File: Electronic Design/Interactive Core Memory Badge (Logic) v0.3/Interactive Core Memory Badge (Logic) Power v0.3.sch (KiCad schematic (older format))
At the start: 18 parts, among them J3 Conn_01x03_Male, J4 Conn_01x02_Male, J5 Conn_01x02_Male, Q1 IRLML6344TRPBF, SW1 SW_DPDT_x2, U1 LD1117S33TR_SOT223

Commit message: Schematic refinement
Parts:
- removed J3: Conn_01x03_Male, symbol Connector:Conn_01x03_Male
- removed J5: Conn_01x02_Male, symbol Connector:Conn_01x02_Male
- added J3: BM03B-PASS-1-TFT__LF__SN_, JST_BM03B-PASS-1-TFT:BM03BPASS1TFTLFSN, symbol BM03B-PASS-1-TFT__LF__SN_:BM03B-PASS-1-TFT__LF__SN_
- added R51, R52: 10k, Resistor_SMD:R_0805_2012Metric, symbol Device:R
- D1: footprint Digikey:DO-214AC -> Diode_SMD:D_SMA_Handsoldering
- J4: footprint (none) -> Connector_PinSocket_2.54mm:PinSocket_1x02_P2.54mm_Vertical_SMD_Pin1Left
- R43: value 0.01 -> 0.001
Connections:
- net labels added: VSW_HALF_VOL_MONITOR
- net labels removed: FEATHER_GND, FEATHER_VBAT, FEATHER_VBUS
- wire segments 51 -> 47
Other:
- note added: "ALL SYSTEM\nSTAR GROUNDING"
- note added: "ALTERNATE CONNECTOR - Generic SMT 2-pin .1” \nheader option for everything else."
- note added: "BOTH MODES REQUIRE:\nVIN must be supplied TO the Teensy\n(because VIN-VUSB is cut) and the \nCore 64 Logic Board provides it here."
- note added: "DIGITAL\nLOGIC GROUND"
- note added: "Diode provides 1.1V drop if using USB power.\n Keeps +VSW close to 4V to reduce 3.3V regulator strain.\n Prevents current flow back to USB and provides \n additional reverse polarity protection."
- note added: "HACKER UPGRADE TO USE FEATHER-TEENSY ADAPTER BOARD REQUIRES:\nA) REPLACE THE ALKALINE/NIMH BATTERY PACK WITH 1S LIPO IN THE SAME POWER PORT, OR THE ALTERNATE PORT.\n -or-\nB) REMOVE THE ALKALINE/NIMH BATTERY PACK AND CONNECT 1S LIPO DIRECTLY TO FEATHER JST-PH BATTERY/CHARGING PORT."
- note added: "HIGH POWER\nSYSTEM GROUND"
- note added: "MODE 2\n USB 5V through Teensy LC or 3.2 \n VUSB is 5V from USB cable."
- note added: "POWER SWITCH AND VOLTAGE MONITOR"
- note added: "REVERSE POLARITY\nPROTECTION"
- note added: "SYSTEM CURRENT\nMEASUREMENT"
- note added: "TEENSY LC OR 3.2 AND ALKALINE/NIMH BATTERY PACK\n*** MUST CUT VIN-VUSB TRACE ON TEENSY ***\nTHIS IS THE STANDARD MANUFACTURED KIT CONFIGURATION"
- note removed: "BOTH MODES REQUIRE:\nVIN must be supplied TO the Teensy and\nthe Core 64 Logic Board provides it here."
- note removed: "DIGITAL LOGIC GROUND"
- note removed: "Diode provides 1.1V drop if using USB power.\n Keeps +VSW close to 4V to reduce 3.3V regulator strain.\n Prevents current flow back to USB and provides additional reverse polarity protection."
- note removed: "HACKER UPGRADE TO USE FEATHER REQUIRES EITHER:\nA) REPLACE THE ALKALINE/NIMH BATTERY PACK WITH 1S LIPO IN THE SAME POWER PORT, OR ONE OF THE ALTERNATE PORTS\n>>> ALTERNATE CONNECTOR 1 - Adafruit (1769) SMT 2-pin JST-PH (used with the Feather and Adafruit batteries)\n>>> ALTERNATE CONNECTOR 2 - Generic SMT 2-pin .1” header option for everything else. \nB) REMOVE THE ALKALINE/NIMH BATTERY PACK AND 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"
- note removed: "MODE 2\n USB 5V through Teensy LC or 3.2 \n VUSB is 5V from USB cable.\n VIN must be supplied TO the Teensy and Core 64 Logic Board provides it."
- note removed: "MODE 3\n USER REPLACED 1S LIPO BATTERY 3.7 OR 4.2V\n THE FEATHER WILL TRY TO CHARGE THE BATTERY AT 100MA WHEN USB POWER IS CONNECTED. \n FAILURE TO USE A 1S LIPO WILL DESTROY THE CHARGER CIRCUIT ON THE FEATHER."
- note removed: "MODE 4\n USB 5V through the Feather.\n Automatically recharges a connected 1s LiPo at 100mA."
- note removed: "POWER SWITCH"
- note removed: "REVERSE POLARITY PROTECTION"
- note removed: "STAR GROUND AS MUCH AS POSSIBLE REVERSE\nPOLARITY FET TO GNDD (DIGITAL) AND GND (POWER)."
- note removed: "SYSTEM CURRENT MEASUREMENT"
- note removed: "TEENSY LC OR 3.2 AND ALKALINE/NIMH BATTERY PACK\n*** MUST CUT VIN-VUSB TRACE ***\nTHIS IS THE STANDARD MANUFACTURED KIT CONFIGURATION"
- note removed: "TO DO: Connect to analog inputs of MCU for self-test and diagnostics."
- note removed: "TO DO: Does Feather receive power to MCU directly from battery?\nDoes Feather require a battery to be connected in order to work?"
- note removed: "TO DO: Teensy and feather power to -Batt or GND? \nDo they need to avoid the reverse polarity detector? \nOr will they interfere?"
- note removed: "TWO ALTERNATIVE POWER MODES SELECTED BY DOUBLE-THROW SWITCH:"
- moved on the sheet: C3, D1, F1, J4, Q1, R1, SW1A, TP1, TP2, TP3, TP4, TP5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

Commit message: Added OLED power solder jumpers
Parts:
- Q1: footprint Package_TO_SOT_SMD:SOT-23 -> Digikey:SOT-23-3
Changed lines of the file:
@@
 F 0 "Q1" V 1701 6650 50  0000 C CNN
 F 1 "IRLML6344TRPBF" V 1794 6650 50  0000 C CNN
-F 2 "Package_TO_SOT_SMD:SOT-23" H 1650 6575 50  0001 L CIN
+F 2 "Digikey:SOT-23-3" H 1650 6575 50  0001 L CIN
 F 3 "https://www.digikey.com/product-detail/en/infineon-technologies/IRLML6344TRPBF/IRLML6344TRPBFCT-ND/2538168" H 1450 6650 50  0001 L CNN
 	1    1450 6650

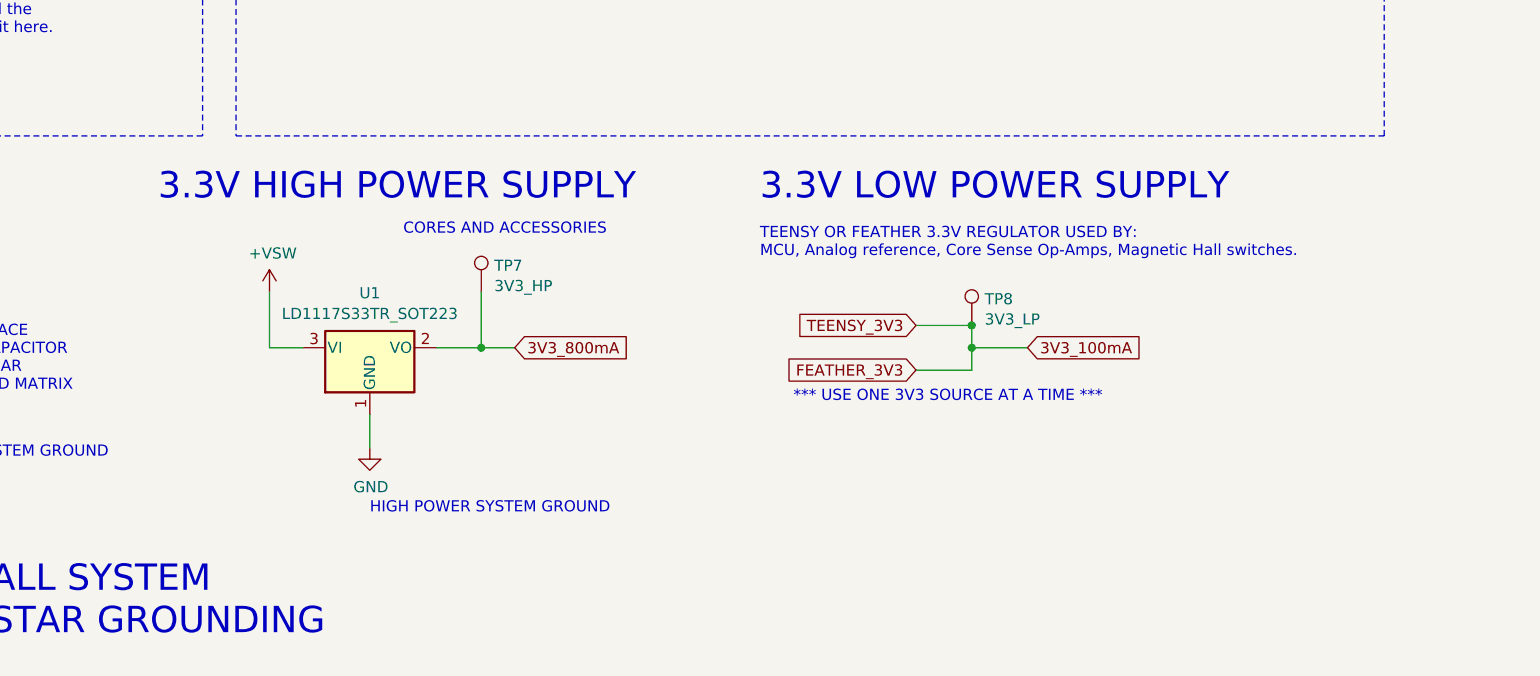
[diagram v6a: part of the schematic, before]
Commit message: Overall PCB layout placements
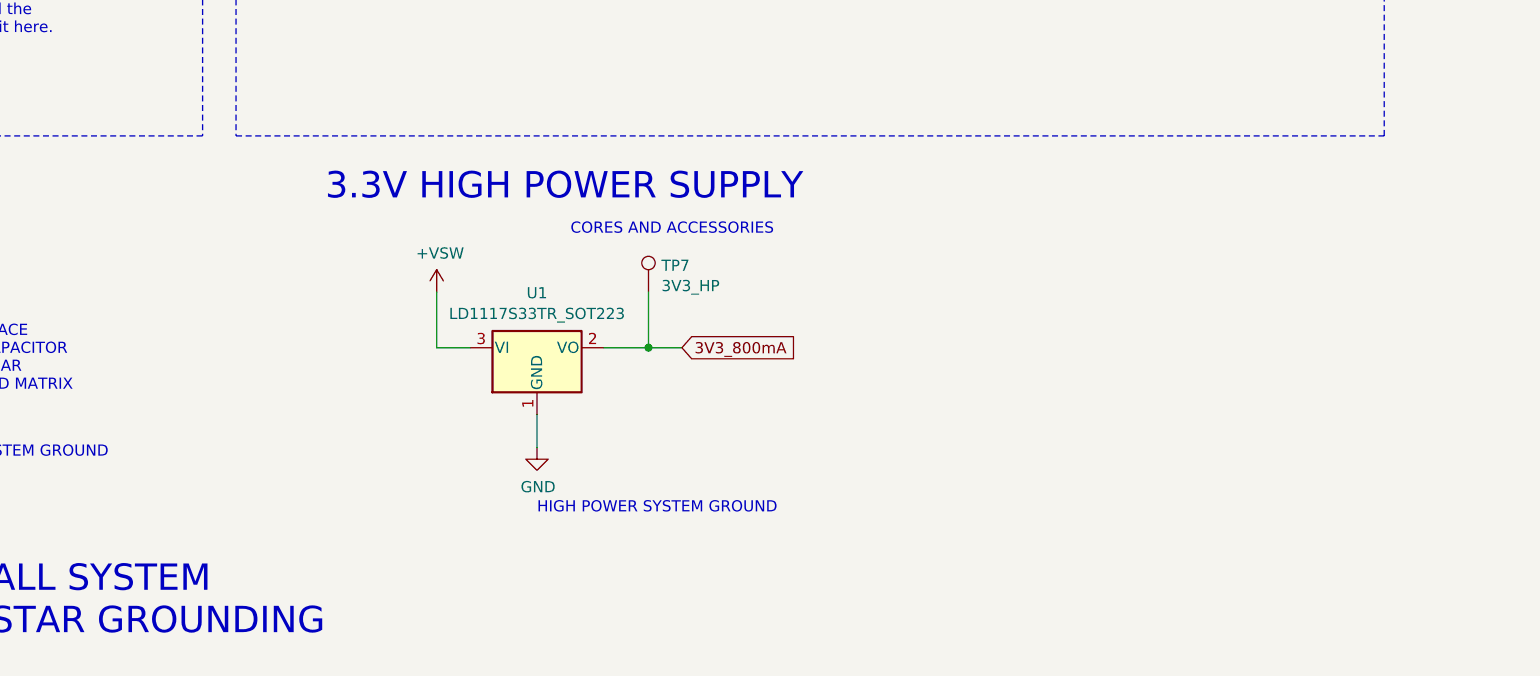
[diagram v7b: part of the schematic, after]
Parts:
- removed TP8: 3V3_LP, TestPoint:TestPoint_Keystone_5000-5004_Miniature, symbol Connector:TestPoint
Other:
- note removed: "*** USE ONE 3V3 SOURCE AT A TIME ***"
- note removed: "3.3V LOW POWER SUPPLY"
- note removed: "TEENSY OR FEATHER 3.3V REGULATOR USED BY:\nMCU, Analog reference, Core Sense Op-Amps, Magnetic Hall switches."
- moved on the sheet: TP7, U1
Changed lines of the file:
@@
 $EndComp
 Wire Wire Line
-	6950 4900 7150 4900
+	7700 4900 7900 4900
 Text GLabel 1000 4900 0    50   Input ~ 0
 5V_USB
@@
 	-1   0    0    1
 $EndComp
-Text Notes 6800 4400 0    50   ~ 0
+Text Notes 7550 4400 0    50   ~ 0
 CORES AND ACCESSORIES
 $Comp
@@
 $EndComp
 Wire Wire Line
-	7150 4900 7300 4900
-Connection ~ 7150 4900
-Wire Wire Line
-	7150 4650 7150 4900
+	7900 4900 8050 4900
+Connection ~ 7900 4900
+Wire Wire Line
+	7900 4650 7900 4900
 $Comp
 L Switch:SW_DPDT_x2 SW1
@@
 L Regulator_Linear:LD1117S33TR_SOT223 U1
 U 1 1 5E7B5B14
-P 6650 4900
+P 7400 4900
 AR Path="/5E7548ED/5E7B5B14" Ref="U1"  Part="1"
 AR Path="/5E755AC8/5D254AE8/5E7B5B14" Ref="U?"  Part="1"
-F 0 "U1" H 6650 5145 50  0000 C CNN
-F 1 "LD1117S33TR_SOT223" H 6650 5052 50  0000 C CNN
-F 2 "Package_TO_SOT_SMD:SOT-223-3_TabPin2" H 6650 5100 50  0001 C CNN
-F 3 "http://www.st.com/st-web-ui/static/active/en/resource/technical/document/datasheet/CD00000544.pdf" H 6750 4650 50  0001 C CNN
-	1    6650 4900
+F 0 "U1" H 7400 5145 50  0000 C CNN
+F 1 "LD1117S33TR_SOT223" H 7400 5052 50  0000 C CNN
+F 2 "Package_TO_SOT_SMD:SOT-223-3_TabPin2" H 7400 5100 50  0001 C CNN
+F 3 "http://www.st.com/st-web-ui/static/active/en/resource/technical/document/datasheet/CD00000544.pdf" H 7500 4650 50  0001 C CNN
+	1    7400 4900
 	1    0    0    -1
 $EndComp
@@
 REVERSE POLARITY\nPROTECTION
 Wire Wire Line
-	6200 4900 6350 4900
+	6950 4900 7100 4900
 Text Notes 750  2200 0    50   ~ 0
 MODE 1\n  BUILT-IN BATTERY PACK (Keystone 2482CN) WITH 4X “AAA” ALKALINE OR NIMH CELLS\n  …or 3-4 “AA” alkaline/NiMh, or 1S LiPo, but the logic board does not recharge these batteries automatically from USB power.\n  CONNECTED TO 3 PIN input for Battery Pack\n  On PCB: SMT CONN, 3 TERM, HORZ, 2mm spacing, detent lock\n  Such as: Keystone 976, JST PA BM03B-PASS-1-TFT(LF)(SN), Adafruit 4391 (JST PH 3-pin aka STEMMA)\n  from KAWEEI Technology CW2001-03T-H01-BD-A,
@@
 Text GLabel 4450 3800 0    50   Input ~ 0
 TEENSY_VIN
-Text GLabel 9100 4800 0    50   Input ~ 0
-TEENSY_3V3
 Text GLabel 1600 3550 0    50   Input ~ 0
 TEENSY_GND
@@
 Text Notes 3950 3500 0    50   ~ 0
 BOTH MODES REQUIRE:\nVIN must be supplied TO the Teensy\n(because VIN-VUSB is cut) and the \nCore 64 Logic Board provides it here.
-Text Notes 8400 4500 0    50   ~ 0
-TEENSY OR FEATHER 3.3V REGULATOR USED BY:\nMCU, Analog reference, Core Sense Op-Amps, Magnetic Hall switches.
-Text GLabel 9100 5000 0    50   Input ~ 0
-FEATHER_3V3
-Text GLabel 9600 4900 2    50   Input ~ 0
-3V3_100mA
-Wire Wire Line
-	9100 4800 9350 4800
-Wire Wire Line
-	9350 4800 9350 4900
-Wire Wire Line
-	9350 4900 9600 4900
-Wire Wire Line
-	9350 4900 9350 5000
-Wire Wire Line
-	9350 5000 9100 5000
-Connection ~ 9350 4900
 $Comp
 L power:+VSW #PWR0113
 U 1 1 5E8659D4
-P 6200 4650
+P 6950 4650
 AR Path="/5E7548ED/5E8659D4" Ref="#PWR0113"  Part="1"
 AR Path="/5E755AC8/5D254AE8/5E8659D4" Ref="#PWR?"  Part="1"
-F 0 "#PWR0113" H 6200 4500 50  0001 C CNN
-F 1 "+VSW" H 6215 4823 50  0000 C CNN
-F 2 "" H 6200 4650 50  0001 C CNN
-F 3 "" H 6200 4650 50  0001 C CNN
-	1    6200 4650
-	1    0    0    -1
-$EndComp
-Wire Wire Line
-	6200 4650 6200 4900
-Text GLabel 7300 4900 2    50   Input ~ 0
+F 0 "#PWR0113" H 6950 4500 50  0001 C CNN
+F 1 "+VSW" H 6965 4823 50  0000 C CNN
+F 2 "" H 6950 4650 50  0001 C CNN
+F 3 "" H 6950 4650 50  0001 C CNN
+	1    6950 4650
+	1    0    0    -1
+$EndComp
+Wire Wire Line
+	6950 4650 6950 4900
+Text GLabel 8050 4900 2    50   Input ~ 0
 3V3_800mA
 Wire Wire Line
@@
 Text Notes 550  4250 0    118  ~ 0
 POWER SWITCH AND VOLTAGE MONITOR
-Text Notes 8400 4250 0    118  ~ 0
-3.3V LOW POWER SUPPLY
-Text Notes 5700 4250 0    118  ~ 0
+Text Notes 6450 4250 0    118  ~ 0
 3.3V HIGH POWER SUPPLY
-$Comp
-L Connector:TestPoint TP8
-U 1 1 5E88D7B5
-P 9350 4800
-AR Path="/5E7548ED/5E88D7B5" Ref="TP8"  Part="1"
-AR Path="/5E755AC8/5D254AE8/5E88D7B5" Ref="TP?"  Part="1"
-F 0 "TP8" H 9408 4918 50  0000 L CNN
-F 1 "3V3_LP" H 9408 4827 50  0000 L CNN
-F 2 "TestPoint:TestPoint_Keystone_5000-5004_Miniature" H 9550 4800 50  0001 C CNN
-F 3 "~" H 9550 4800 50  0001 C CNN
-	1    9350 4800
-	1    0    0    -1
-$EndComp
 $Comp
 L Connector:TestPoint TP7
 U 1 1 5E88DBA6
-P 7150 4650
+P 7900 4650
 AR Path="/5E7548ED/5E88DBA6" Ref="TP7"  Part="1"
 AR Path="/5E755AC8/5D254AE8/5E88DBA6" Ref="TP?"  Part="1"
-F 0 "TP7" H 7208 4768 50  0000 L CNN
-F 1 "3V3_HP" H 7208 4677 50  0000 L CNN
-F 2 "TestPoint:TestPoint_Keystone_5000-5004_Miniature" H 7350 4650 50  0001 C CNN
-F 3 "~" H 7350 4650 50  0001 C CNN
-	1    7150 4650
+F 0 "TP7" H 7958 4768 50  0000 L CNN
+F 1 "3V3_HP" H 7958 4677 50  0000 L CNN
+F 2 "TestPoint:TestPoint_Keystone_5000-5004_Miniature" H 8100 4650 50  0001 C CNN
+F 3 "~" H 8100 4650 50  0001 C CNN
+	1    7900 4650
 	1    0    0    -1
 $EndComp
@@
 L power:GND #PWR0116
 U 1 1 5E8C4F56
-P 6650 5350
+P 7400 5350
 AR Path="/5E7548ED/5E8C4F56" Ref="#PWR0116"  Part="1"
 AR Path="/5E755AC8/5D254AE8/5E8C4F56" Ref="#PWR?"  Part="1"
-F 0 "#PWR0116" H 6650 5100 50  0001 C CNN
-F 1 "GND" H 6655 5175 50  0000 C CNN
-F 2 "" H 6650 5350 50  0001 C CNN
-F 3 "" H 6650 5350 50  0001 C CNN
-	1    6650 5350
-	1    0    0    -1
-$EndComp
-Wire Wire Line
-	6650 5200 6650 5350
+F 0 "#PWR0116" H 7400 5100 50  0001 C CNN
+F 1 "GND" H 7405 5175 50  0000 C CNN
+F 2 "" H 7400 5350 50  0001 C CNN
+F 3 "" H 7400 5350 50  0001 C CNN
+	1    7400 5350
+	1    0    0    -1
+$EndComp
+Wire Wire Line
+	7400 5200 7400 5350
 Text Notes 2650 6200 0    118  ~ 0
 SYSTEM CURRENT\nMEASUREMENT
@@
 	1    0    0    -1
 $EndComp
-Connection ~ 9350 4800
 $Comp
 L Device:CP1_Small C?
@@
 	1    0    0    -1
 $EndComp
-Text Notes 6650 5650 0    50   ~ 0
+Text Notes 7400 5650 0    50   ~ 0
 HIGH POWER SYSTEM GROUND
 Text Notes 4400 5400 0    50   ~ 0
@@
 Text Notes 2050 3850 0    50   ~ 0
 HIGH POWER SYSTEM GROUND
-Text Notes 8550 5150 0    50   ~ 0
-*** USE ONE 3V3 SOURCE AT A TIME ***
 Text Notes 4000 4650 0    50   ~ 0
 LED ARRAY, TEENSY VIN

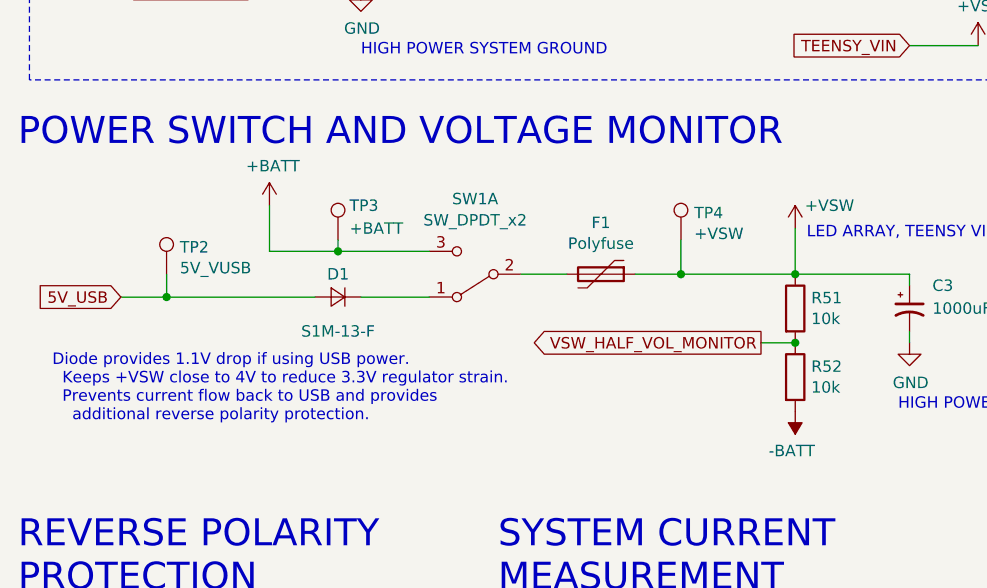
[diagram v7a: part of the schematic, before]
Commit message: Add I2C Hall sensor, data sheets, sample code
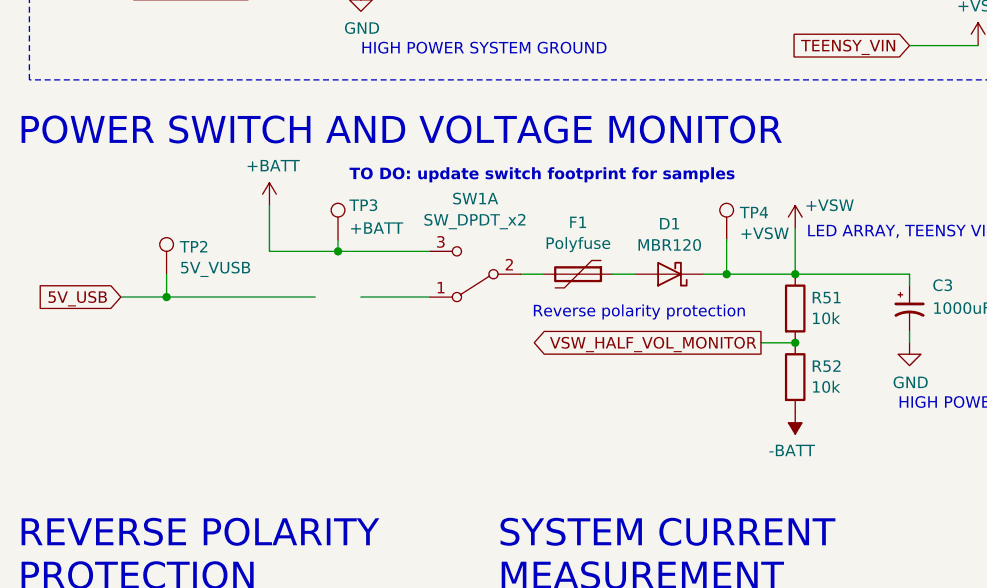
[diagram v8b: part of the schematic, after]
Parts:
- removed D1: S1M-13-F, Diode_SMD:D_SMA_Handsoldering, symbol Device:D_Small
- added D1: MBR120, Diode_SMD:D_SOD-123F, symbol Diode:MBR0520
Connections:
- wire segments 42 -> 43
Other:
- note added: "Reverse polarity protection"
- note added: "TO DO: update switch footprint for samples"
- note removed: "Diode provides 1.1V drop if using USB power.\n Keeps +VSW close to 4V to reduce 3.3V regulator strain.\n Prevents current flow back to USB and provides \n additional reverse polarity protection."
- moved on the sheet: F1, TP4
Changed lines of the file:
@@
 L Device:Polyfuse F1
 U 1 1 5D3009B0
-P 3100 4800
+P 3000 4800
 AR Path="/5E7548ED/5D3009B0" Ref="F1"  Part="1"
 AR Path="/5E755AC8/5D254AE8/5D3009B0" Ref="F?"  Part="1"
-F 0 "F1" V 2875 4800 50  0000 C CNN
-F 1 "Polyfuse" V 2966 4800 50  0000 C CNN
-F 2 "Fuse:Fuse_0805_2012Metric" H 3150 4600 50  0001 L CNN
-F 3 "~" H 3100 4800 50  0001 C CNN
-	1    3100 4800
+F 0 "F1" V 2775 4800 50  0000 C CNN
+F 1 "Polyfuse" V 2866 4800 50  0000 C CNN
+F 2 "Fuse:Fuse_0805_2012Metric" H 3050 4600 50  0001 L CNN
+F 3 "~" H 3000 4800 50  0001 C CNN
+	1    3000 4800
 	0    1    1    0
 $EndComp
 Wire Wire Line
-	2750 4800 2950 4800
+	2750 4800 2850 4800
 $Comp
 L power:+VSW #PWR0102
@@
 L Connector:TestPoint TP4
 U 1 1 5D48E646
-P 3450 4650
+P 3650 4650
 AR Path="/5E7548ED/5D48E646" Ref="TP4"  Part="1"
 AR Path="/5E755AC8/5D254AE8/5D48E646" Ref="TP?"  Part="1"
-F 0 "TP4" H 3508 4768 50  0000 L CNN
-F 1 "+VSW" H 3508 4677 50  0000 L CNN
-F 2 "TestPoint:TestPoint_Keystone_5000-5004_Miniature" H 3650 4650 50  0001 C CNN
-F 3 "~" H 3650 4650 50  0001 C CNN
-	1    3450 4650
+F 0 "TP4" H 3708 4768 50  0000 L CNN
+F 1 "+VSW" H 3708 4677 50  0000 L CNN
+F 2 "TestPoint:TestPoint_Keystone_5000-5004_Miniature" H 3850 4650 50  0001 C CNN
+F 3 "~" H 3850 4650 50  0001 C CNN
+	1    3650 4650
 	1    0    0    -1
 $EndComp
@@
 	-1   0    0    1
 $EndComp
-$Comp
-L Device:D_Small D1
-U 1 1 5E9B647B
-P 1950 4900
-AR Path="/5E7548ED/5E9B647B" Ref="D1"  Part="1"
-AR Path="/5E755AC8/5D254AE8/5E9B647B" Ref="D?"  Part="1"
-F 0 "D1" H 1950 4800 50  0000 C CNN
-F 1 "S1M-13-F" H 1950 5050 50  0000 C CNN
-F 2 "Diode_SMD:D_SMA_Handsoldering" H 1950 4900 50  0001 C CNN
-F 3 "~" H 1950 4900 50  0001 C CNN
-	1    1950 4900
-	-1   0    0    1
-$EndComp
-Text Notes 700  5450 0    50   ~ 0
-Diode provides 1.1V drop if using USB power.\n  Keeps +VSW close to 4V to reduce 3.3V regulator strain.\n  Prevents current flow back to USB and provides \n    additional reverse polarity protection.
+Text Notes 2800 5000 0    50   ~ 0
+Reverse polarity protection
 $Comp
 L Regulator_Linear:LD1117S33TR_SOT223 U1
@@
 $EndComp
 Wire Wire Line
-	3450 4800 3250 4800
-Wire Wire Line
-	3950 4800 3450 4800
-Connection ~ 3450 4800
-Wire Wire Line
-	3450 4650 3450 4800
+	3650 4800 3550 4800
+Wire Wire Line
+	3950 4800 3650 4800
+Connection ~ 3650 4800
+Wire Wire Line
+	3650 4650 3650 4800
 $Comp
 L power:GND #PWR0116
@@
 Wire Wire Line
 	1800 2550 2400 2550
+$Comp
+L Diode:MBR0520 D1
+U 1 1 5E87F7F2
+P 3400 4800
+F 0 "D1" H 3400 4581 50  0000 C CNN
+F 1 "MBR120" H 3400 4674 50  0000 C CNN
+F 2 "Diode_SMD:D_SOD-123F" H 3400 4625 50  0001 C CNN
+F 3 "https://www.digikey.com/product-detail/en/on-semiconductor/MBR120VLSFT1G/MBR120VLSFT1GOSCT-ND/893874" H 3400 4800 50  0001 C CNN
+	1    3400 4800
+	-1   0    0    1
+$EndComp
+Text Notes 2000 4400 0    50   ~ 10
+TO DO: update switch footprint for samples
+Wire Wire Line
+	3250 4800 3150 4800
 $EndSCHEMATC
